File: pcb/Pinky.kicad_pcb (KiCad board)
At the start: 2 copper layers, 142.2 x 120.5 mm, 78 parts, among them J1 MJ-4PP-9, P1 i2c-pin, P2 i2c-pin, SW1 RESET_SW, SW10 SW_PUSH, SW11 SW_PUSH, SW12 SW_PUSH, SW13 SW_PUSH, SW14 SW_PUSH, SW15 SW_PUSH, SW16 SW_PUSH, SW17 SW_PUSH, SW18 SW_PUSH, SW19 SW_PUSH, SW2 SW_PUSH, SW20 SW_PUSH, SW21 SW_PUSH, SW22 SW_PUSH, SW23 SW_PUSH, SW24 SW_PUSH, SW25 SW_PUSH, SW26 SW_PUSH, SW27 SW_PUSH, SW28 SW_PUSH, SW29 SW_PUSH, SW3 SW_PUSH, SW30 SW_PUSH, SW31 SW_PUSH, SW32 SW_PUSH, SW33 SW_PUSH, SW4 SW_PUSH, SW5 SW_PUSH, SW6 SW_PUSH, SW7 SW_PUSH, SW8 SW_PUSH, SW9 SW_PUSH, U1 ProMicro

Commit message: sent to allpcb
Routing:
- net Net-(J1-PadB): track 112.1 -> 122.7 mm, vias 1 -> 0
- net row2: track 191.6 -> 185.5 mm
- net GND: track 178.1 -> 172.4 mm, vias 29 -> 35
- net row1: track 203.6 -> 205.7 mm
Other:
- rule pad_to_mask_clearance: 0.051 -> 0.2

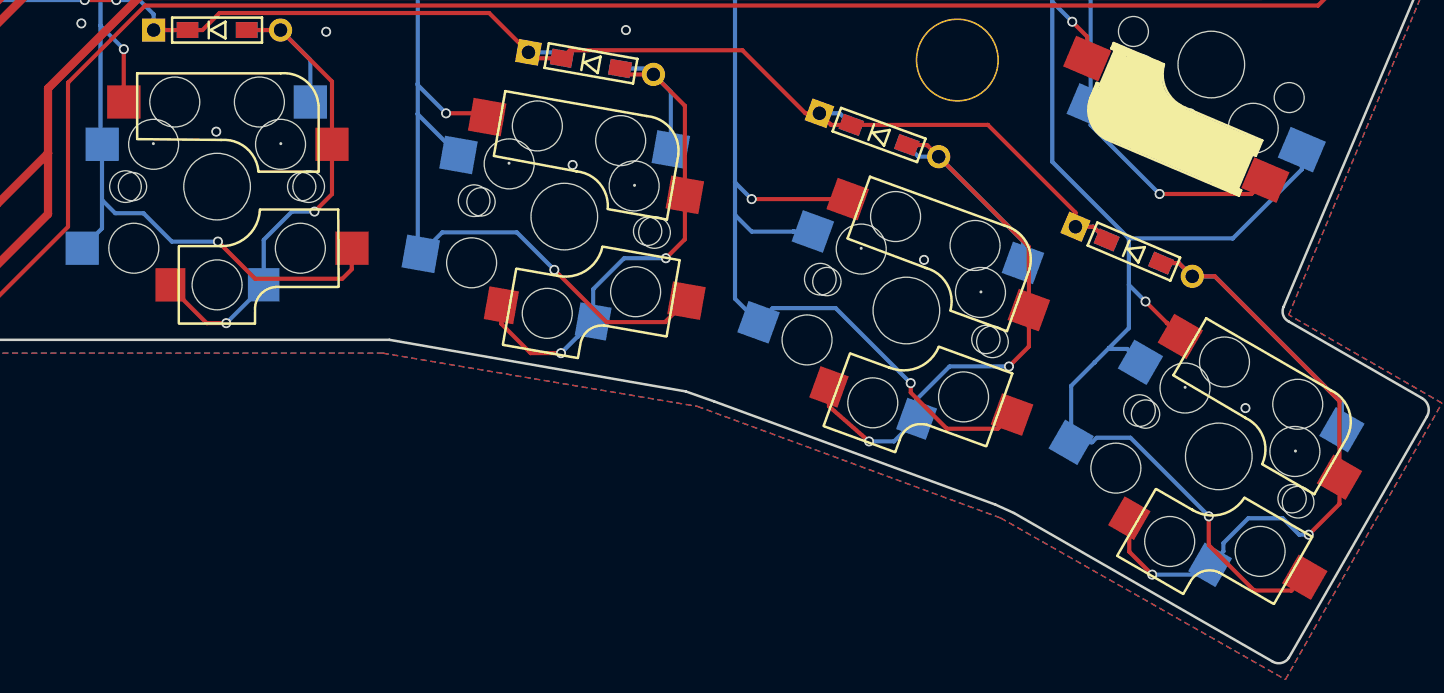
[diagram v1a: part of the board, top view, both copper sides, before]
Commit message: 0.1mm の精度の設定を全て消したつもり。
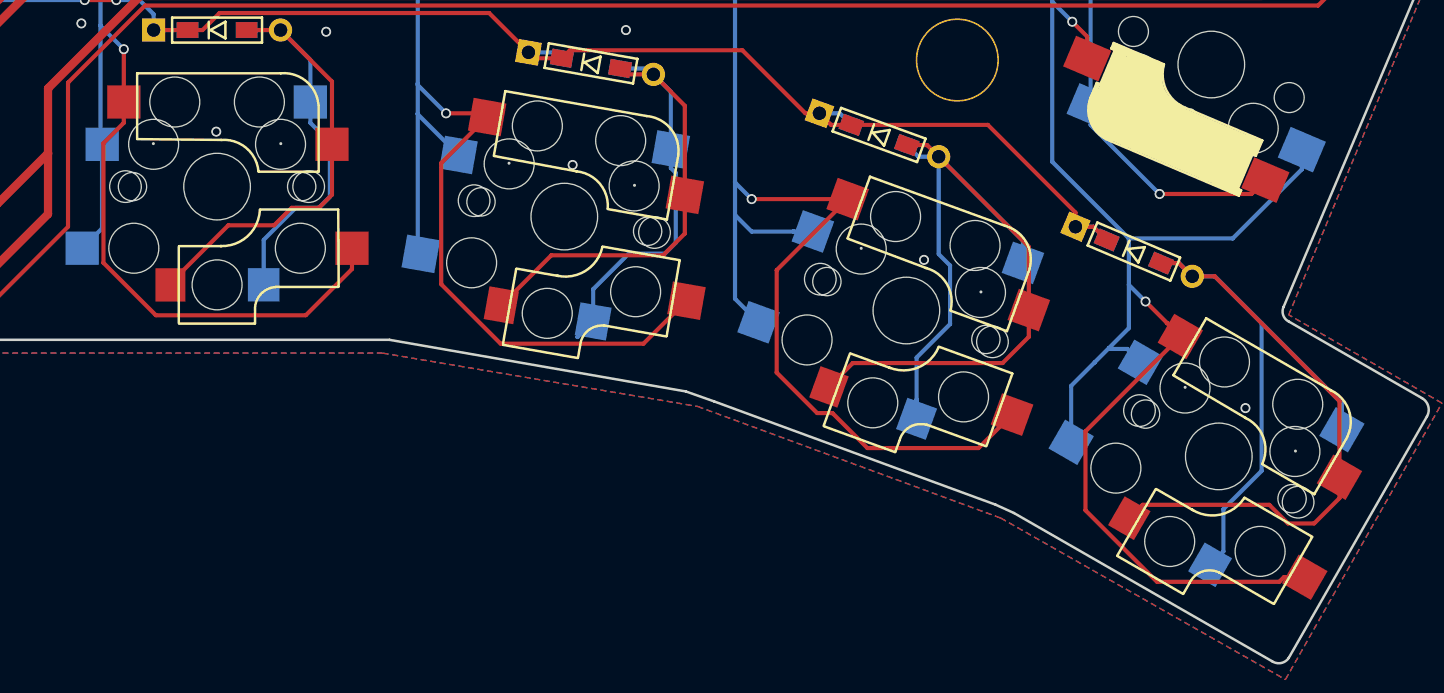
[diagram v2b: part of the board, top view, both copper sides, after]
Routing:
- net Net-(D27-Pad2): track 43.6 -> 57.3 mm, vias 2 -> 0
- net Net-(D32-Pad2): track 54.5 -> 66.0 mm, vias 2 -> 0
- net Net-(D22-Pad2): track 36.8 -> 47.6 mm, vias 2 -> 0
- net Net-(D17-Pad2): track 35.9 -> 46.4 mm, vias 2 -> 0
- net col3: track 256.4 -> 266.8 mm, vias 7 -> 6
- net col5: track 291.5 -> 301.2 mm, vias 7 -> 6
- net col4: track 270.5 -> 279.7 mm, vias 7 -> 6
- net col6: track 307.4 -> 316.0 mm, vias 8 -> 7
